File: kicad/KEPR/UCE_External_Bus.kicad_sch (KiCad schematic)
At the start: 5 parts, among them J10 Conn_02x40_Odd_Even, J6 Conn_02x20_Odd_Even, J7 Conn_02x08_Odd_Even, J8 Conn_01x08_Pin, J9 Conn_02x40_Odd_Even

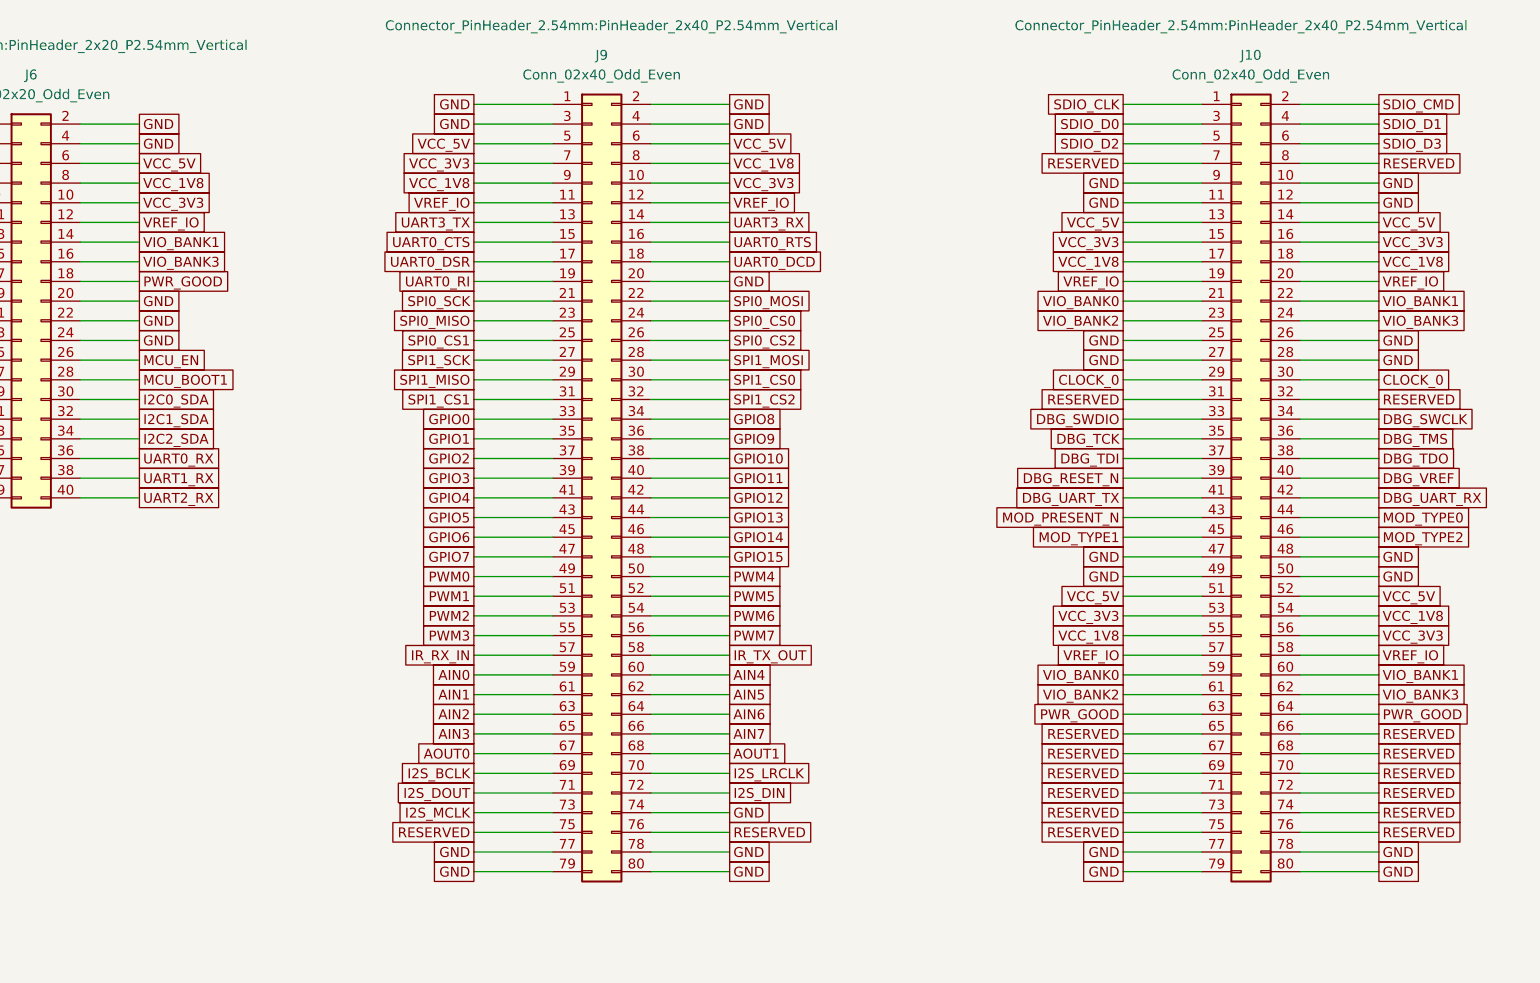
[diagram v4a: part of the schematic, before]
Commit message: Iniciado a distribuição das vias.
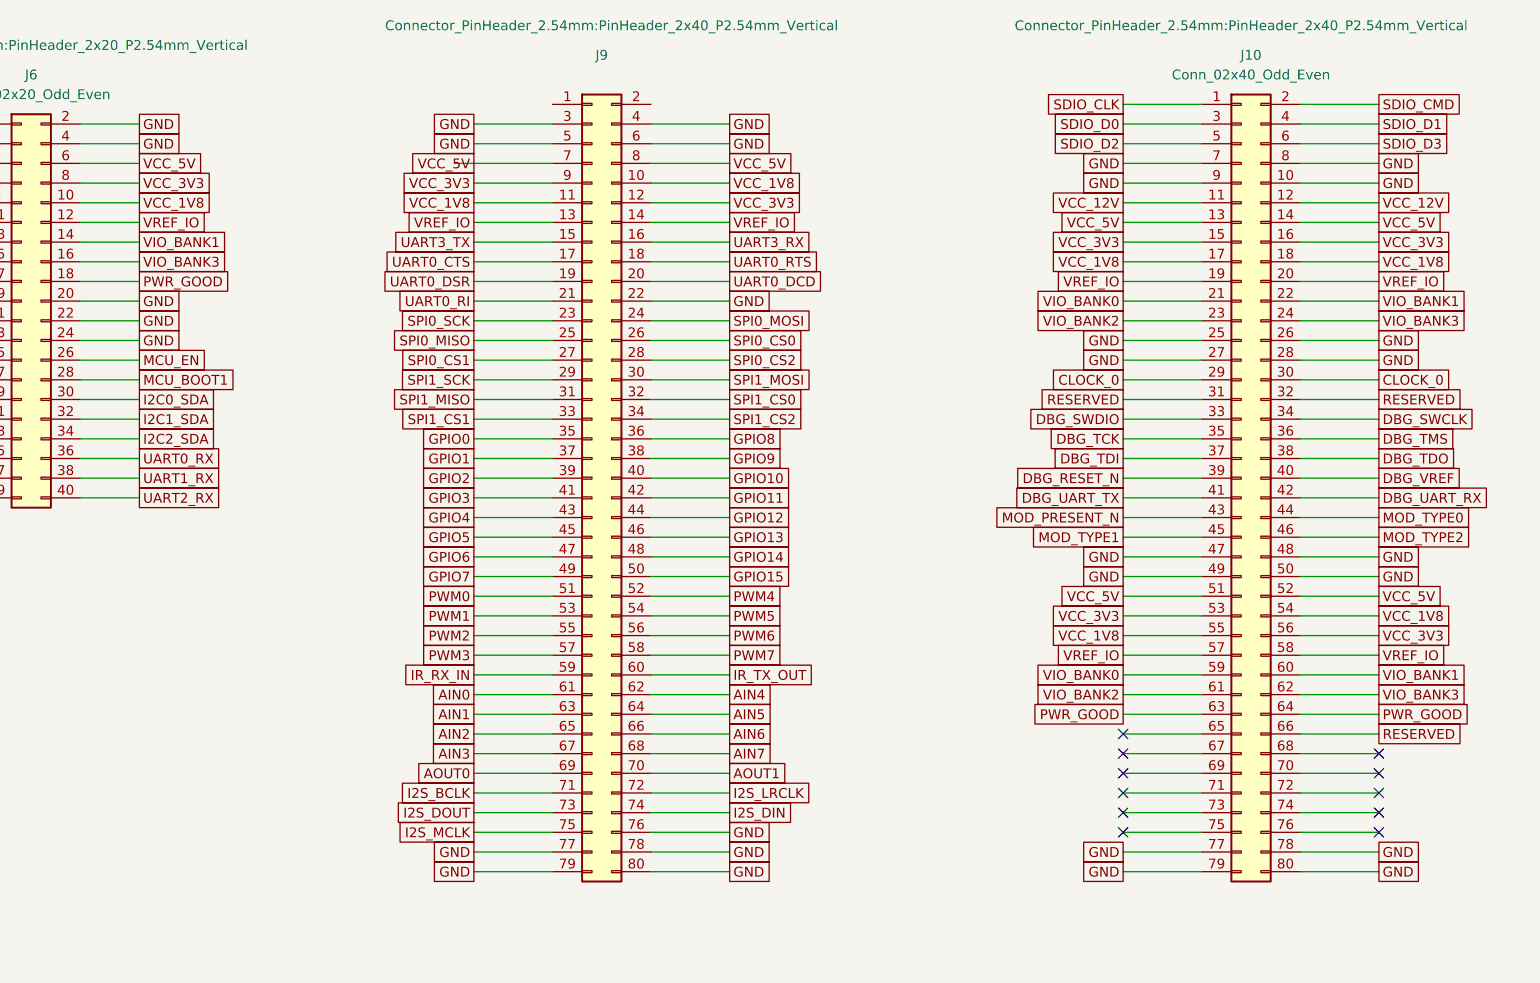
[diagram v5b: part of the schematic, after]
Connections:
- net AIN0: now also J9.61 (Pin_61); no longer J9.59 (Pin_59)
- net AIN1: now also J9.63 (Pin_63); no longer J9.61 (Pin_61)
- net AIN2: now also J9.65 (Pin_65); no longer J9.63 (Pin_63)
- net AIN3: now also J9.67 (Pin_67); no longer J9.65 (Pin_65)
- net AIN4: now also J9.62 (Pin_62); no longer J9.60 (Pin_60)
- net AIN5: now also J9.64 (Pin_64); no longer J9.62 (Pin_62)
- net AIN6: now also J9.66 (Pin_66); no longer J9.64 (Pin_64)
- net AIN7: now also J9.68 (Pin_68); no longer J9.66 (Pin_66)
- net AOUT0: now also J9.69 (Pin_69); no longer J9.67 (Pin_67)
- net AOUT1: now also J9.70 (Pin_70); no longer J9.68 (Pin_68)
- net GND: now also J10.7 (Pin_7), J10.8 (Pin_8), J9.22 (Pin_22), J9.5 (Pin_5), J9.6 (Pin_6), J9.76 (Pin_76); no longer J10.11 (Pin_11), J10.12 (Pin_12), J9.1 (Pin_1), J9.2 (Pin_2), J9.20 (Pin_20), J9.74 (Pin_74)
- net GPIO0: now also J9.35 (Pin_35); no longer J9.33 (Pin_33)
- net GPIO1: now also J9.37 (Pin_37); no longer J9.35 (Pin_35)
- net GPIO10: now also J9.40 (Pin_40); no longer J9.38 (Pin_38)
- net GPIO11: now also J9.42 (Pin_42); no longer J9.40 (Pin_40)
- net GPIO12: now also J9.44 (Pin_44); no longer J9.42 (Pin_42)
- net GPIO13: now also J9.46 (Pin_46); no longer J9.44 (Pin_44)
- net GPIO14: now also J9.48 (Pin_48); no longer J9.46 (Pin_46)
- net GPIO15: now also J9.50 (Pin_50); no longer J9.48 (Pin_48)
- net GPIO2: now also J9.39 (Pin_39); no longer J9.37 (Pin_37)
- net GPIO3: now also J9.41 (Pin_41); no longer J9.39 (Pin_39)
- net GPIO4: now also J9.43 (Pin_43); no longer J9.41 (Pin_41)
- net GPIO5: now also J9.45 (Pin_45); no longer J9.43 (Pin_43)
- net GPIO6: now also J9.47 (Pin_47); no longer J9.45 (Pin_45)
- net GPIO7: now also J9.49 (Pin_49); no longer J9.47 (Pin_47)
- net GPIO8: now also J9.36 (Pin_36); no longer J9.34 (Pin_34)
- net GPIO9: now also J9.38 (Pin_38); no longer J9.36 (Pin_36)
- net I2S_BCLK: now also J9.71 (Pin_71); no longer J9.69 (Pin_69)
- net I2S_DIN: now also J9.74 (Pin_74); no longer J9.72 (Pin_72)
- net I2S_DOUT: now also J9.73 (Pin_73); no longer J9.71 (Pin_71)
- net I2S_LRCLK: now also J9.72 (Pin_72); no longer J9.70 (Pin_70)
- net I2S_MCLK: now also J9.75 (Pin_75); no longer J9.73 (Pin_73)
- net IR_RX_IN: now also J9.59 (Pin_59); no longer J9.57 (Pin_57)
- net IR_TX_OUT: now also J9.60 (Pin_60); no longer J9.58 (Pin_58)
- net PWM0: now also J9.51 (Pin_51); no longer J9.49 (Pin_49)
- net PWM1: now also J9.53 (Pin_53); no longer J9.51 (Pin_51)
- net PWM2: now also J9.55 (Pin_55); no longer J9.53 (Pin_53)
- net PWM3: now also J9.57 (Pin_57); no longer J9.55 (Pin_55)
- net PWM4: now also J9.52 (Pin_52); no longer J9.50 (Pin_50)
- net PWM5: now also J9.54 (Pin_54); no longer J9.52 (Pin_52)
- net PWM6: now also J9.56 (Pin_56); no longer J9.54 (Pin_54)
- net PWM7: now also J9.58 (Pin_58); no longer J9.56 (Pin_56)
- net RESERVED: no longer J10.65 (Pin_65), J10.67 (Pin_67), J10.68 (Pin_68), J10.69 (Pin_69), J10.7 (Pin_7), J10.70 (Pin_70), J10.71 (Pin_71), J10.72 (Pin_72), J10.73 (Pin_73), J10.74 (Pin_74), J10.75 (Pin_75), J10.76 (Pin_76), J10.8 (Pin_8), J9.75 (Pin_75), J9.76 (Pin_76)
- net SPI0_CS0: now also J9.26 (Pin_26); no longer J9.24 (Pin_24)
- net SPI0_CS1: now also J9.27 (Pin_27); no longer J9.25 (Pin_25)
- net SPI0_CS2: now also J9.28 (Pin_28); no longer J9.26 (Pin_26)
- net SPI0_MISO: now also J9.25 (Pin_25); no longer J9.23 (Pin_23)
- net SPI0_MOSI: now also J9.24 (Pin_24); no longer J9.22 (Pin_22)
- net SPI0_SCK: now also J9.23 (Pin_23); no longer J9.21 (Pin_21)
- net SPI1_CS0: now also J9.32 (Pin_32); no longer J9.30 (Pin_30)
- net SPI1_CS1: now also J9.33 (Pin_33); no longer J9.31 (Pin_31)
- net SPI1_CS2: now also J9.34 (Pin_34); no longer J9.32 (Pin_32)
- net SPI1_MISO: now also J9.31 (Pin_31); no longer J9.29 (Pin_29)
- net SPI1_MOSI: now also J9.30 (Pin_30); no longer J9.28 (Pin_28)
- net SPI1_SCK: now also J9.29 (Pin_29); no longer J9.27 (Pin_27)
- net UART0_CTS: now also J9.17 (Pin_17); no longer J9.15 (Pin_15)
- net UART0_DCD: now also J9.20 (Pin_20); no longer J9.18 (Pin_18)
- net UART0_DSR: now also J9.19 (Pin_19); no longer J9.17 (Pin_17)
- net UART0_RI: now also J9.21 (Pin_21); no longer J9.19 (Pin_19)
- net UART0_RTS: now also J9.18 (Pin_18); no longer J9.16 (Pin_16)
- net UART3_RX: now also J9.16 (Pin_16); no longer J9.14 (Pin_14)
- net UART3_TX: now also J9.15 (Pin_15); no longer J9.13 (Pin_13)
- net VCC_1V8: now also J6.10 (Pin_10), J9.10 (Pin_10), J9.11 (Pin_11); no longer J6.8 (Pin_8), J9.8 (Pin_8), J9.9 (Pin_9)
- net VCC_3V3: now also J6.8 (Pin_8), J9.12 (Pin_12), J9.9 (Pin_9); no longer J6.10 (Pin_10), J9.10 (Pin_10), J9.7 (Pin_7)
- net VCC_5V: now also J9.7 (Pin_7), J9.8 (Pin_8); no longer J9.5 (Pin_5), J9.6 (Pin_6)
- net VREF_IO: now also J9.13 (Pin_13), J9.14 (Pin_14); no longer J9.11 (Pin_11), J9.12 (Pin_12)
- new net VCC_12V: J10.11 (Pin_11), J10.12 (Pin_12)
- no-connect marks 0 -> 11

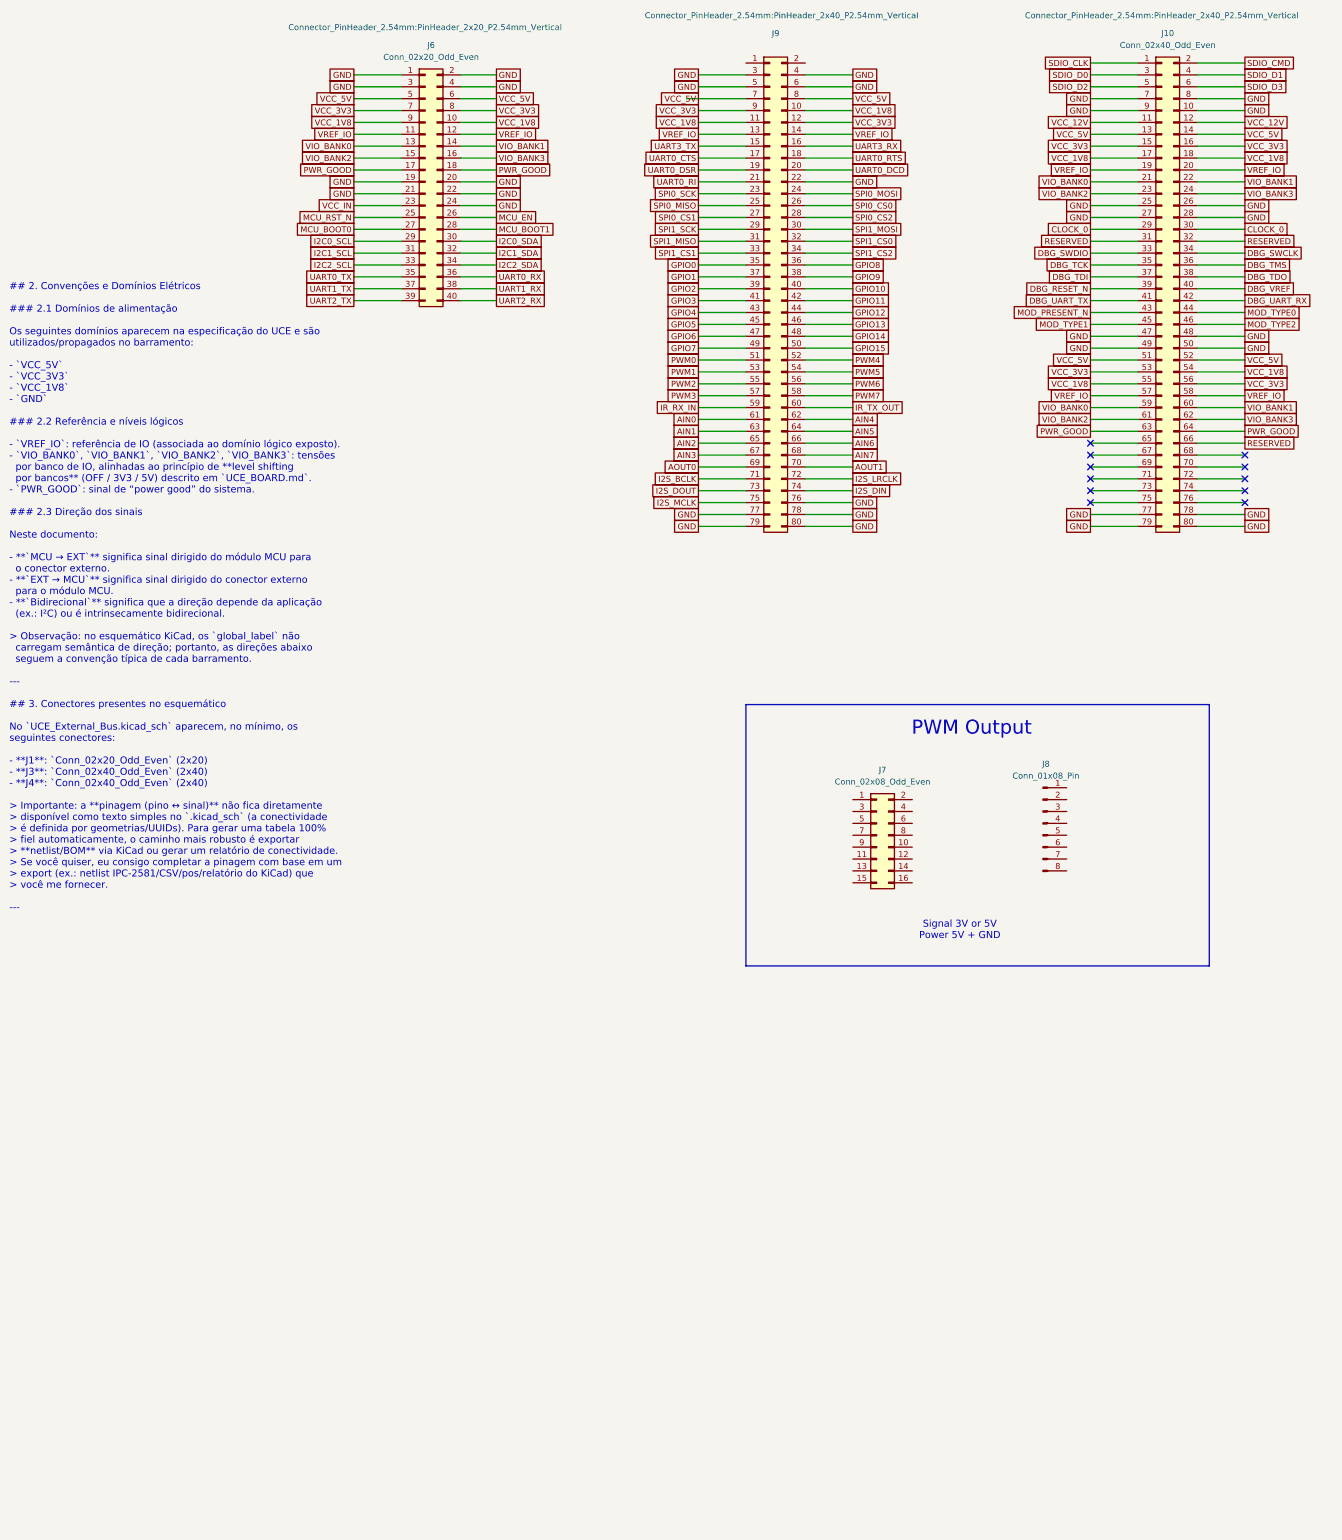
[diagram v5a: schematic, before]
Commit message: Diversos ajustes no barramento e ampliação das trilhas na PCB
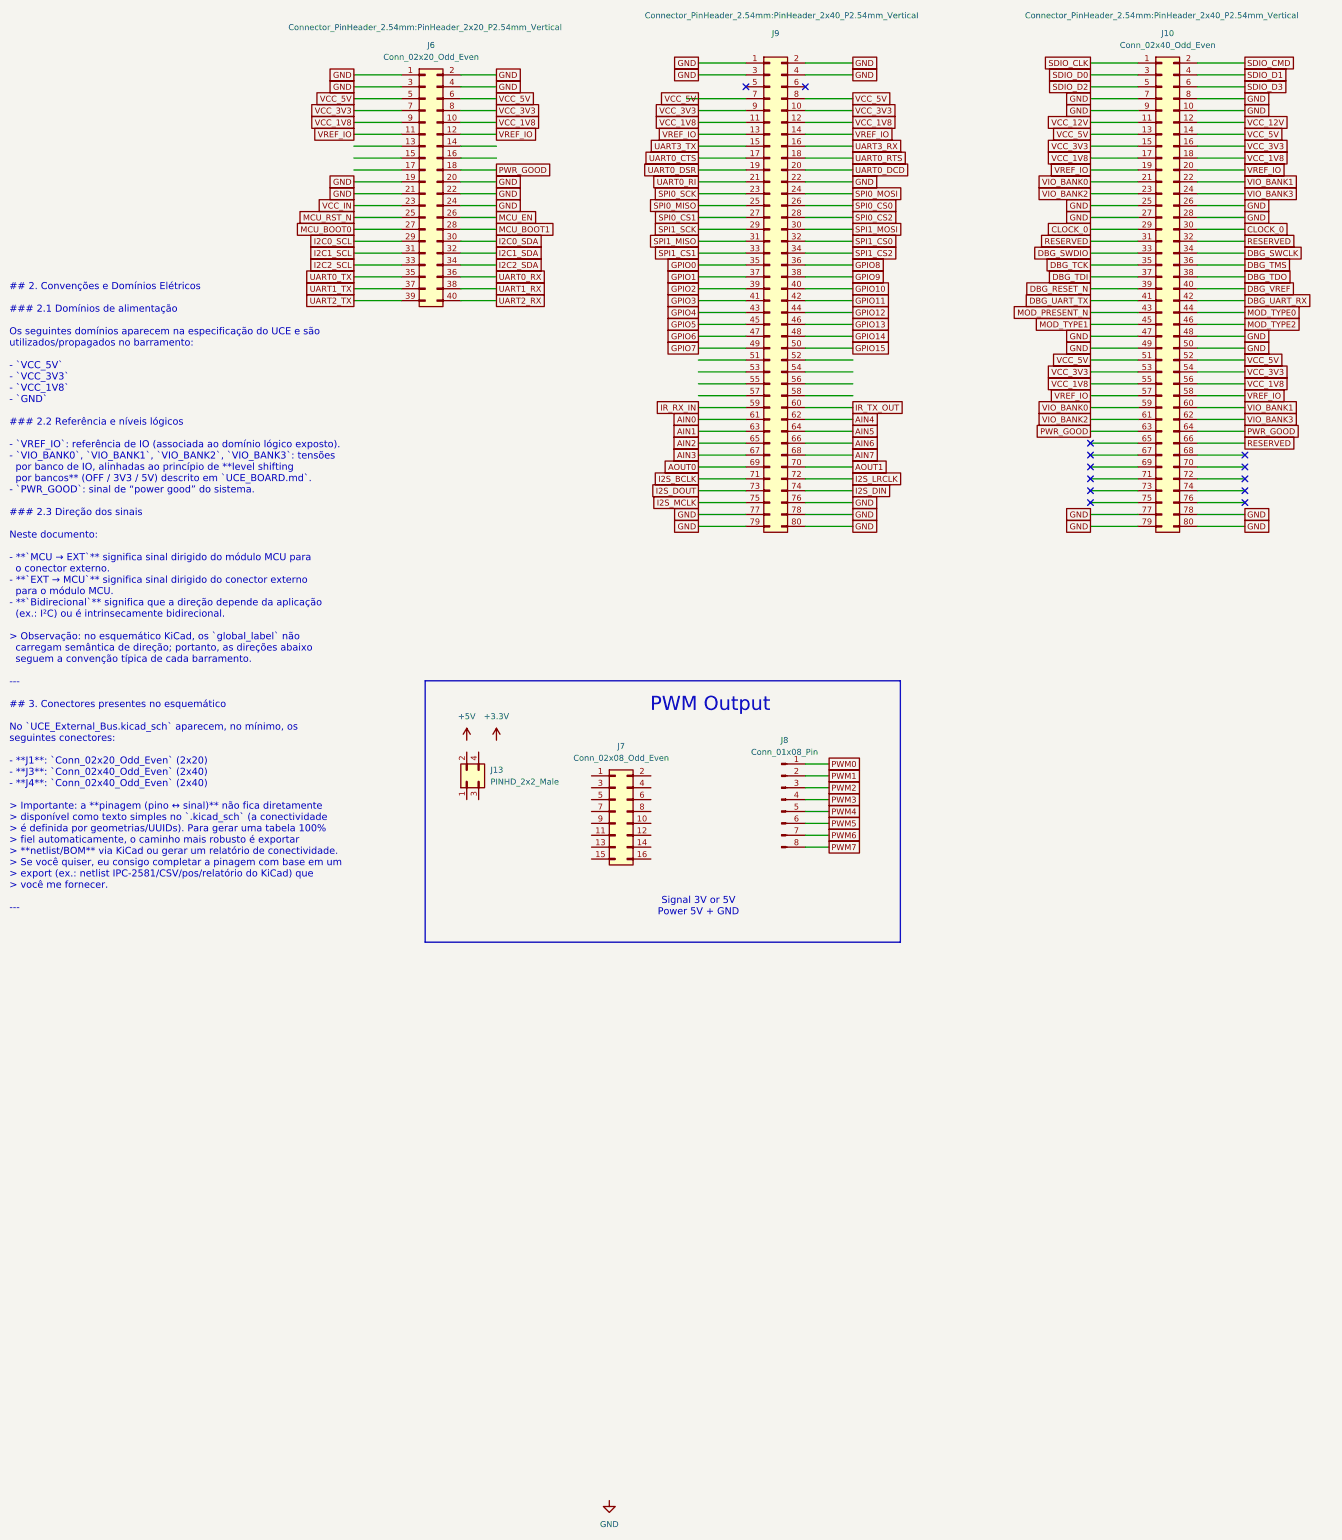
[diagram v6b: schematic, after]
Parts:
- added J13: PINHD_2x2_Male, Connector_PinHeader_2.54mm:PinHeader_2x02_P2.54mm_Vertical, symbol PCM_SL_Pin_Headers:PINHD_2x2_Male
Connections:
- net GND: now also J9.1 (Pin_1), J9.2 (Pin_2); no longer J9.5 (Pin_5), J9.6 (Pin_6)
- net PWM0: now also J8.1 (Pin_1); no longer J9.51 (Pin_51)
- net PWM1: now also J8.2 (Pin_2); no longer J9.53 (Pin_53)
- net PWM2: now also J8.3 (Pin_3); no longer J9.55 (Pin_55)
- net PWM3: now also J8.4 (Pin_4); no longer J9.57 (Pin_57)
- net PWM4: now also J8.5 (Pin_5); no longer J9.52 (Pin_52)
- net PWM5: now also J8.6 (Pin_6); no longer J9.54 (Pin_54)
- net PWM6: now also J8.7 (Pin_7); no longer J9.56 (Pin_56)
- net PWM7: now also J8.8 (Pin_8); no longer J9.58 (Pin_58)
- net PWR_GOOD: no longer J6.17 (Pin_17)
- net VCC_1V8: now also J10.56 (Pin_56), J9.12 (Pin_12); no longer J10.54 (Pin_54), J9.10 (Pin_10)
- net VCC_3V3: now also J10.54 (Pin_54), J9.10 (Pin_10); no longer J10.56 (Pin_56), J9.12 (Pin_12)
- net VIO_BANK0: no longer J6.13 (Pin_13)
- net VIO_BANK1: no longer J6.14 (Pin_14)
- net VIO_BANK2: no longer J6.15 (Pin_15)
- net VIO_BANK3: no longer J6.16 (Pin_16)
- no-connect marks 11 -> 13
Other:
- moved on the sheet: J7, J8
